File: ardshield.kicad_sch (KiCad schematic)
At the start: 35 parts, among them J1 Conn_01x10_Pin, J2 Conn_01x08_Pin, J3 Conn_01x06_Pin, J4 Conn_01x08_Pin, J5 AudioJack2_SwitchT, Q1 BCP56, U1 MCP6002-xSN

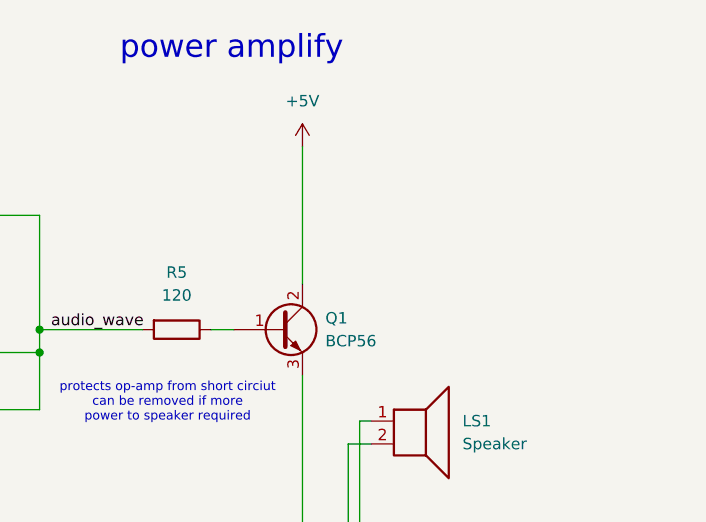
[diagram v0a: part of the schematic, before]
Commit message: added capacitor
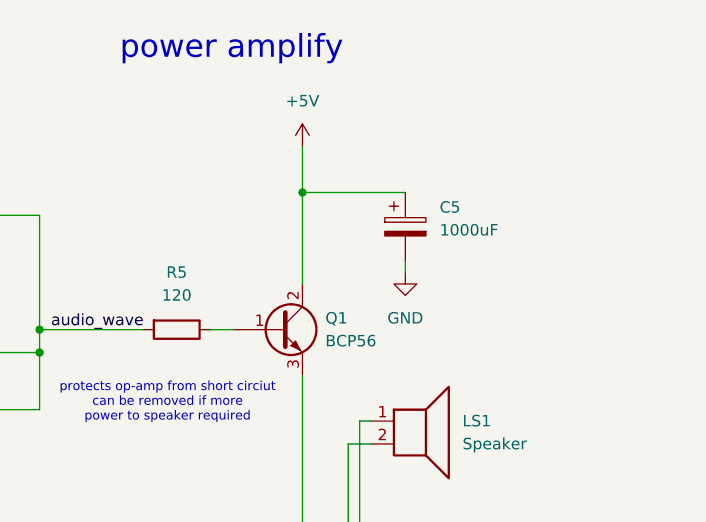
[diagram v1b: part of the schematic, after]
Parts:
- added C5: 1000uF, symbol Device:C_Polarized
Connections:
- net +5V: now also C5.1
- net GND: now also C5.2
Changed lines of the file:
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@@
 	)
 	(junction
+		(at 247.65 43.18)
+		(diameter 0)
+		(color 0 0 0 0)
+	)
+	(junction
 		(at 158.75 130.81)
 		(diameter 0)
@@
 	(wire
 		(pts
-			(xy 247.65 38.1) (xy 247.65 53.34)
+			(xy 247.65 38.1) (xy 247.65 43.18)
+		)
+		(stroke
+			(width 0)
+			(type default)
+		)
+	)
+	(wire
+		(pts
+			(xy 247.65 43.18) (xy 259.08 43.18)
 		)
 		(stroke
@@
 	(wire
 		(pts
+			(xy 259.08 50.8) (xy 259.08 52.07)
+		)
+		(stroke
+			(width 0)
+			(type default)
+		)
+	)
+	(wire
+		(pts
 			(xy 194.31 58.42) (xy 198.12 58.42)
 		)
@@
 	(wire
 		(pts
+			(xy 247.65 43.18) (xy 247.65 53.34)
+		)
+		(stroke
+			(width 0)
+			(type default)
+		)
+	)
+	(wire
+		(pts
 			(xy 143.51 130.81) (xy 143.51 133.35)
 		)
@@
 	)
 	(symbol
+		(lib_id "Device:C_Polarized")
+		(at 259.08 46.99 0)
+		(unit 1)
+		(exclude_from_sim no)
+		(in_bom yes)
+		(on_board yes)
+		(dnp no)
+		(fields_autoplaced yes)
+		(property "Reference" "C5"
+			(at 262.89 44.8309 0)
+			(effects
+				(font
+					(size 1.27 1.27)
+				)
+				(justify left)
+			)
+		)
+		(property "Value" "1000uF"
+			(at 262.89 47.3709 0)
+			(effects
+				(font
+					(size 1.27 1.27)
+				)
+				(justify left)
+			)
+		)
+		(property "Footprint" ""
+			(at 260.0452 50.8 0)
+			(effects
+				(font
+					(size 1.27 1.27)
+				)
+				(hide yes)
+			)
+		)
+		(property "Datasheet" "~"
+			(at 259.08 46.99 0)
+			(effects
+				(font
+					(size 1.27 1.27)
+				)
+				(hide yes)
+			)
+		)
+		(property "Description" "Polarized capacitor"
+			(at 259.08 46.99 0)
+			(effects
+				(font
+					(size 1.27 1.27)
+				)
+				(hide yes)
+			)
+		)
+		(pin "2"
+		)
+		(pin "1"
+		)
+		(instances
+			(project "ardshield"
+				(path "/bbb5f21f-dcbf-4531-a2fe-6f09b6cf6630"
+					(reference "C5")
+					(unit 1)
+				)
+			)
+		)
+	)
+	(symbol
 		(lib_id "power:GND")
 		(at 143.51 149.86 0)
@@
 					(unit 1)
 				)
+			)
+		)
+	)
+	(symbol
+		(lib_id "power:GND")
+		(at 259.08 52.07 0)
+		(unit 1)
+		(exclude_from_sim no)
+		(in_bom yes)
+		(on_board yes)
+		(dnp no)
+		(fields_autoplaced yes)
+		(property "Reference" "#PWR012"
+			(at 259.08 58.42 0)
+			(effects
+				(font
+					(size 1.27 1.27)
+				)
+				(hide yes)
+			)
+		)
+		(property "Value" "GND"
+			(at 259.08 57.15 0)
+			(effects
+				(font
+					(size 1.27 1.27)
+				)
+			)
+		)
+		(property "Footprint" ""
+			(at 259.08 52.07 0)
+			(effects
+				(font
+					(size 1.27 1.27)
+				)
+				(hide yes)
+			)
+		)
+		(property "Datasheet" ""
+			(at 259.08 52.07 0)
+			(effects
+				(font
+					(size 1.27 1.27)
+				)
+				(hide yes)
+			)
+		)
+		(property "Description" "Power symbol creates a global label with name \"GND\" , ground"
+			(at 259.08 52.07 0)
+			(effects
+				(font
+					(size 1.27 1.27)
+				)
+				(hide yes)
+			)
+		)
+		(pin "1"
+		)
+		(instances
+			(project "ardshield"
+				(path "/bbb5f21f-dcbf-4531-a2fe-6f09b6cf6630"
+					(reference "#PWR012")
+					(unit 1)
+				)
